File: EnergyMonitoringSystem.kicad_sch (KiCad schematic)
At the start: 0 parts

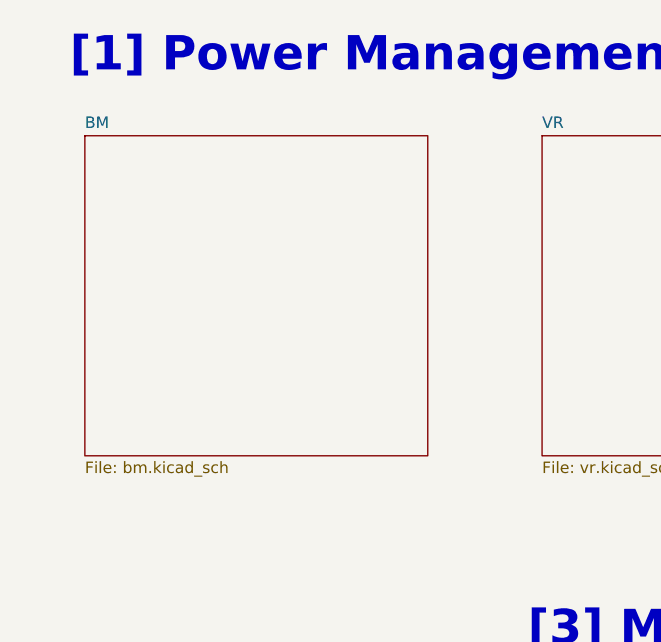
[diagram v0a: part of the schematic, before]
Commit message: only usb powered
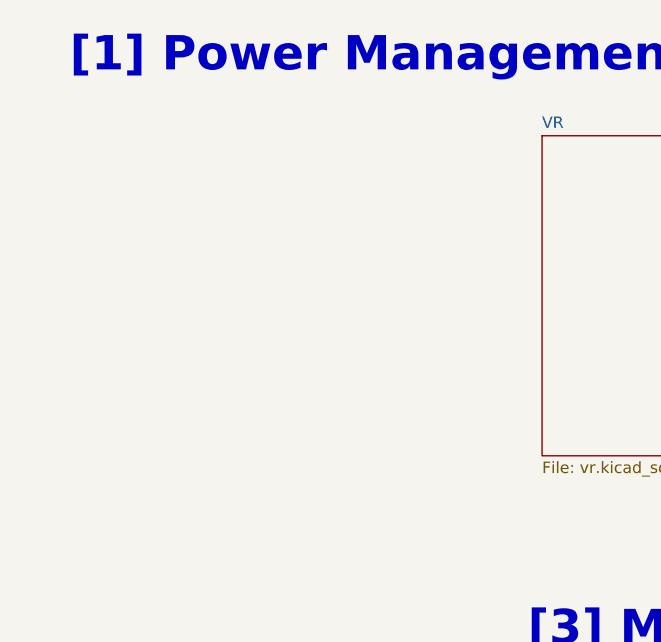
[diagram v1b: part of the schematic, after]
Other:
- removed sheet BM
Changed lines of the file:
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@@
 			(project "EnergyMonitoringSystem"
 				(path "/e660428c-c9b7-476c-8ac8-2d419f233469"
-					(page "7")
+					(page "6")
 				)
 			)
@@
 			(project "EnergyMonitoringSystem"
 				(path "/e660428c-c9b7-476c-8ac8-2d419f233469"
-					(page "4")
+					(page "2")
 				)
 			)
@@
 	)
 	(sheet
-		(at 25.4 36.83)
-		(size 38.1 35.56)
-		(fields_autoplaced yes)
-		(stroke
-			(width 0.1524)
-			(type solid)
-		)
-		(fill
-			(color 0 0 0 0.0000)
-		)
-		(property "Sheetname" "BM"
-			(at 25.4 36.1184 0)
-			(effects
-				(font
-					(size 1.27 1.27)
-				)
-				(justify left bottom)
-			)
-		)
-		(property "Sheetfile" "bm.kicad_sch"
-			(at 25.4 72.9746 0)
-			(effects
-				(font
-					(size 1.27 1.27)
-				)
-				(justify left top)
-			)
-		)
-		(instances
-			(project "EnergyMonitoringSystem"
-				(path "/e660428c-c9b7-476c-8ac8-2d419f233469"
-					(page "2")
-				)
-			)
-		)
-	)
-	(sheet
 		(at 76.2 99.06)
 		(size 39.37 36.83)
@@
 			(project "EnergyMonitoringSystem"
 				(path "/e660428c-c9b7-476c-8ac8-2d419f233469"
-					(page "6")
+					(page "4")
 				)
 			)

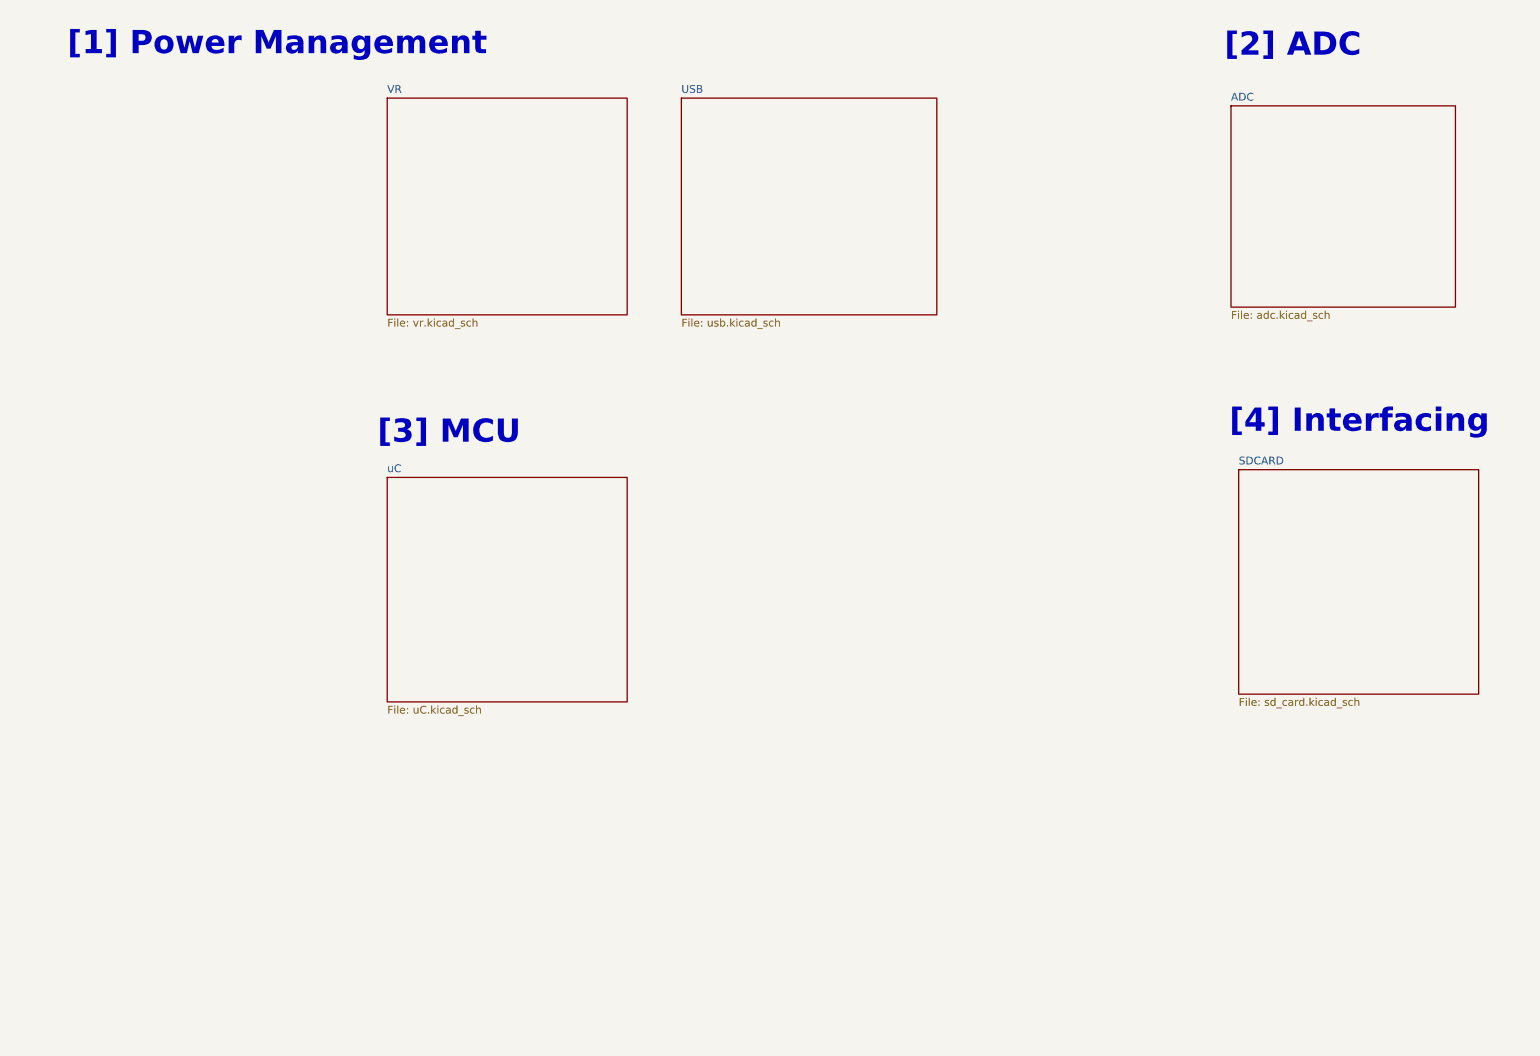
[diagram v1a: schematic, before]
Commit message: components with distributor links added
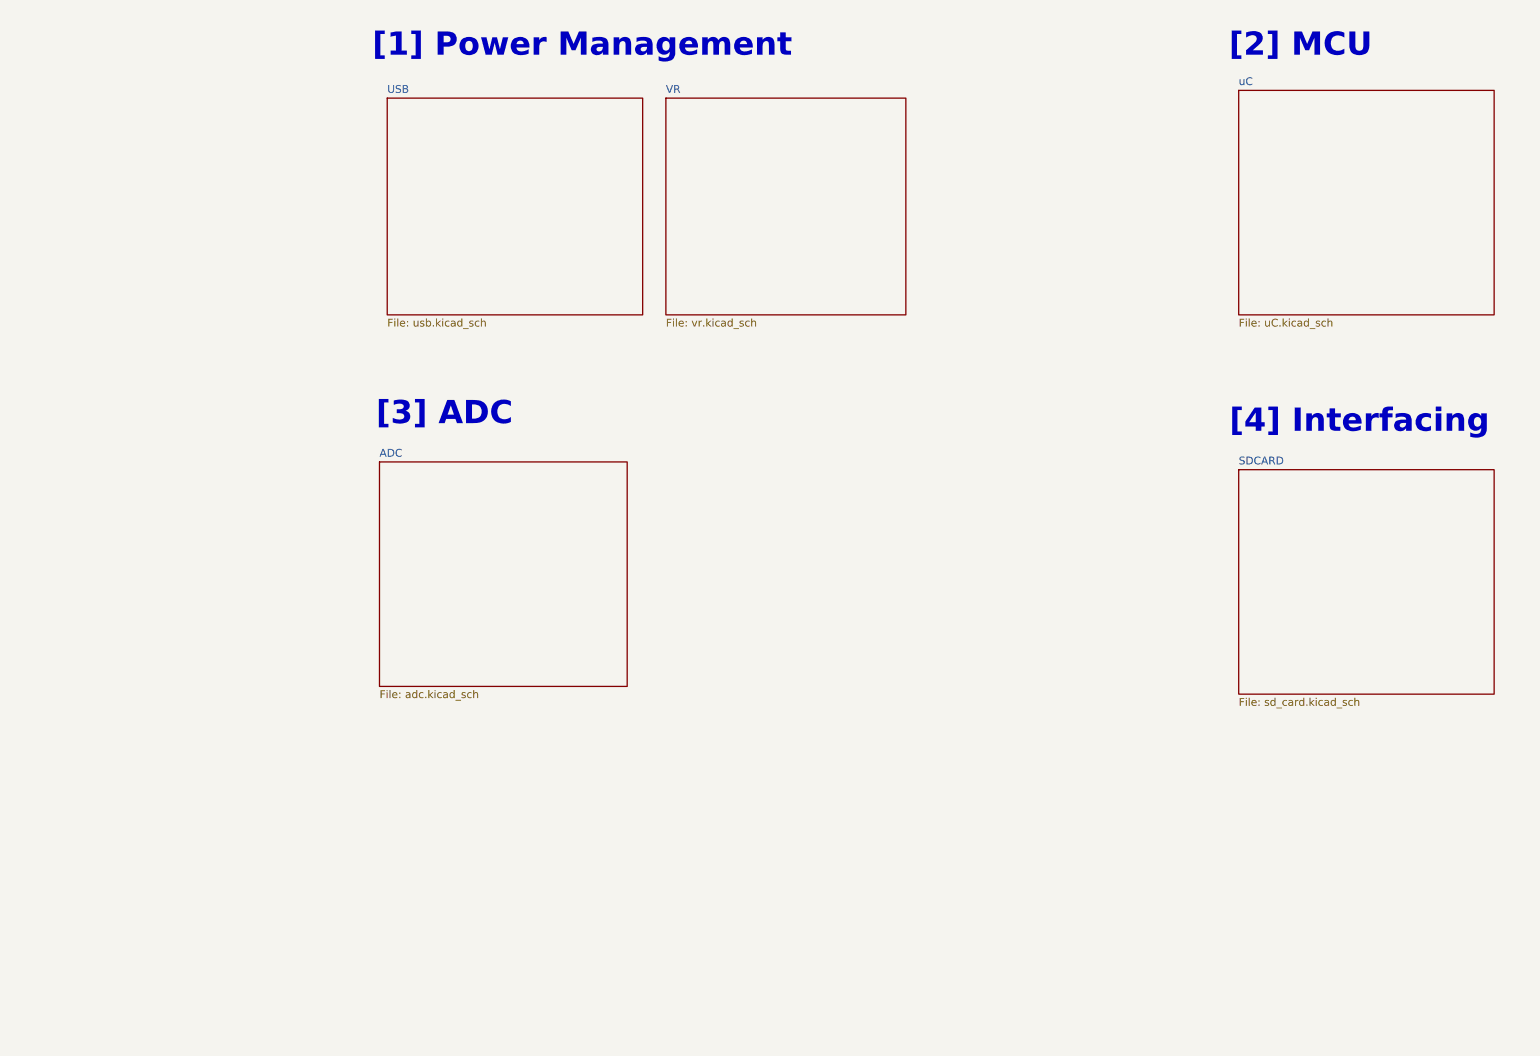
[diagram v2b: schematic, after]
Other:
- note added: "[2] MCU"
- note added: "[3] ADC"
- note removed: "[2] ADC"
- note removed: "[3] MCU"
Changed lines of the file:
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@@
 	(text "[1] Power Management\n"
 		(exclude_from_sim no)
-		(at 58.166 27.94 0)
-		(effects
-			(font
-				(size 3.81 3.81)
-				(thickness 1.016)
-				(bold yes)
-			)
-		)
-	)
-	(text "[2] ADC\n"
-		(exclude_from_sim no)
-		(at 224.79 28.194 0)
-		(effects
-			(font
-				(size 3.81 3.81)
-				(thickness 1.016)
-				(bold yes)
-			)
-		)
-	)
-	(text "[3] MCU\n"
-		(exclude_from_sim no)
-		(at 86.36 91.694 0)
+		(at 108.204 28.194 0)
+		(effects
+			(font
+				(size 3.81 3.81)
+				(thickness 1.016)
+				(bold yes)
+			)
+		)
+	)
+	(text "[3] ADC\n"
+		(exclude_from_sim no)
+		(at 85.598 88.646 0)
+		(effects
+			(font
+				(size 3.81 3.81)
+				(thickness 1.016)
+				(bold yes)
+			)
+		)
+	)
+	(text "[2] MCU\n"
+		(exclude_from_sim no)
+		(at 226.06 28.194 0)
 		(effects
 			(font
@@
 	(sheet
 		(at 215.9 97.79)
-		(size 39.37 36.83)
+		(size 41.91 36.83)
 		(fields_autoplaced yes)
 		(stroke
@@
 	)
 	(sheet
+		(at 121.92 36.83)
+		(size 39.37 35.56)
+		(fields_autoplaced yes)
+		(stroke
+			(width 0.1524)
+			(type solid)
+		)
+		(fill
+			(color 0 0 0 0.0000)
+		)
+		(property "Sheetname" "VR"
+			(at 121.92 36.1184 0)
+			(effects
+				(font
+					(size 1.27 1.27)
+				)
+				(justify left bottom)
+			)
+		)
+		(property "Sheetfile" "vr.kicad_sch"
+			(at 121.92 72.9746 0)
+			(effects
+				(font
+					(size 1.27 1.27)
+				)
+				(justify left top)
+			)
+		)
+		(instances
+			(project "EnergyMonitoringSystem"
+				(path "/e660428c-c9b7-476c-8ac8-2d419f233469"
+					(page "3")
+				)
+			)
+		)
+	)
+	(sheet
 		(at 76.2 36.83)
-		(size 39.37 35.56)
-		(fields_autoplaced yes)
-		(stroke
-			(width 0.1524)
-			(type solid)
-		)
-		(fill
-			(color 0 0 0 0.0000)
-		)
-		(property "Sheetname" "VR"
+		(size 41.91 35.56)
+		(fields_autoplaced yes)
+		(stroke
+			(width 0.1524)
+			(type solid)
+		)
+		(fill
+			(color 0 0 0 0.0000)
+		)
+		(property "Sheetname" "USB"
 			(at 76.2 36.1184 0)
 			(effects
@@
 			)
 		)
-		(property "Sheetfile" "vr.kicad_sch"
+		(property "Sheetfile" "usb.kicad_sch"
 			(at 76.2 72.9746 0)
 			(effects
@@
 			(project "EnergyMonitoringSystem"
 				(path "/e660428c-c9b7-476c-8ac8-2d419f233469"
-					(page "3")
-				)
-			)
-		)
-	)
-	(sheet
-		(at 124.46 36.83)
-		(size 41.91 35.56)
-		(fields_autoplaced yes)
-		(stroke
-			(width 0.1524)
-			(type solid)
-		)
-		(fill
-			(color 0 0 0 0.0000)
-		)
-		(property "Sheetname" "USB"
-			(at 124.46 36.1184 0)
-			(effects
-				(font
-					(size 1.27 1.27)
-				)
-				(justify left bottom)
-			)
-		)
-		(property "Sheetfile" "usb.kicad_sch"
-			(at 124.46 72.9746 0)
-			(effects
-				(font
-					(size 1.27 1.27)
-				)
-				(justify left top)
-			)
-		)
-		(instances
-			(project "EnergyMonitoringSystem"
-				(path "/e660428c-c9b7-476c-8ac8-2d419f233469"
 					(page "2")
 				)
@@
 	)
 	(sheet
-		(at 214.63 38.1)
-		(size 36.83 33.02)
+		(at 74.93 96.52)
+		(size 40.64 36.83)
 		(fields_autoplaced yes)
 		(stroke
@@
 		)
 		(property "Sheetname" "ADC"
-			(at 214.63 37.3884 0)
+			(at 74.93 95.8084 0)
 			(effects
 				(font
@@
 		)
 		(property "Sheetfile" "adc.kicad_sch"
-			(at 214.63 71.7046 0)
+			(at 74.93 133.9346 0)
 			(effects
 				(font
@@
 	)
 	(sheet
-		(at 76.2 99.06)
-		(size 39.37 36.83)
+		(at 215.9 35.56)
+		(size 41.91 36.83)
 		(fields_autoplaced yes)
 		(stroke
@@
 		)
 		(property "Sheetname" "uC"
-			(at 76.2 98.3484 0)
+			(at 215.9 34.8484 0)
 			(effects
 				(font
@@
 		)
 		(property "Sheetfile" "uC.kicad_sch"
-			(at 76.2 136.4746 0)
-			(effects
-				(font
+			(at 215.9 72.9746 0)
+			(effects
+				(font

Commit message: v2.0 started
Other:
- added sheet uCMain (uCMain.kicad_sch)
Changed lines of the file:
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@@
 			(project "EnergyMonitoringSystem"
 				(path "/e660428c-c9b7-476c-8ac8-2d419f233469"
-					(page "6")
+					(page "7")
 				)
 			)
@@
 			(effects
 				(font
+					(size 1.27 1.27)
+				)
+				(justify left top)
+			)
+		)
+		(instances
+			(project "EnergyMonitoringSystem"
+				(path "/e660428c-c9b7-476c-8ac8-2d419f233469"
+					(page "6")
+				)
+			)
+		)
+	)
+	(sheet
+		(at 127 96.52)
+		(size 38.1 36.83)
+		(fields_autoplaced yes)
+		(stroke
+			(width 0.1524)
+			(type solid)
+		)
+		(fill
+			(color 0 0 0 0.0000)
+		)
+		(property "Sheetname" "uCMain"
+			(at 127 95.8084 0)
+			(effects
+				(font
+					(size 1.27 1.27)
+				)
+				(justify left bottom)
+			)
+		)
+		(property "Sheetfile" "uCMain.kicad_sch"
+			(at 127 133.9346 0)
+			(effects
+				(font

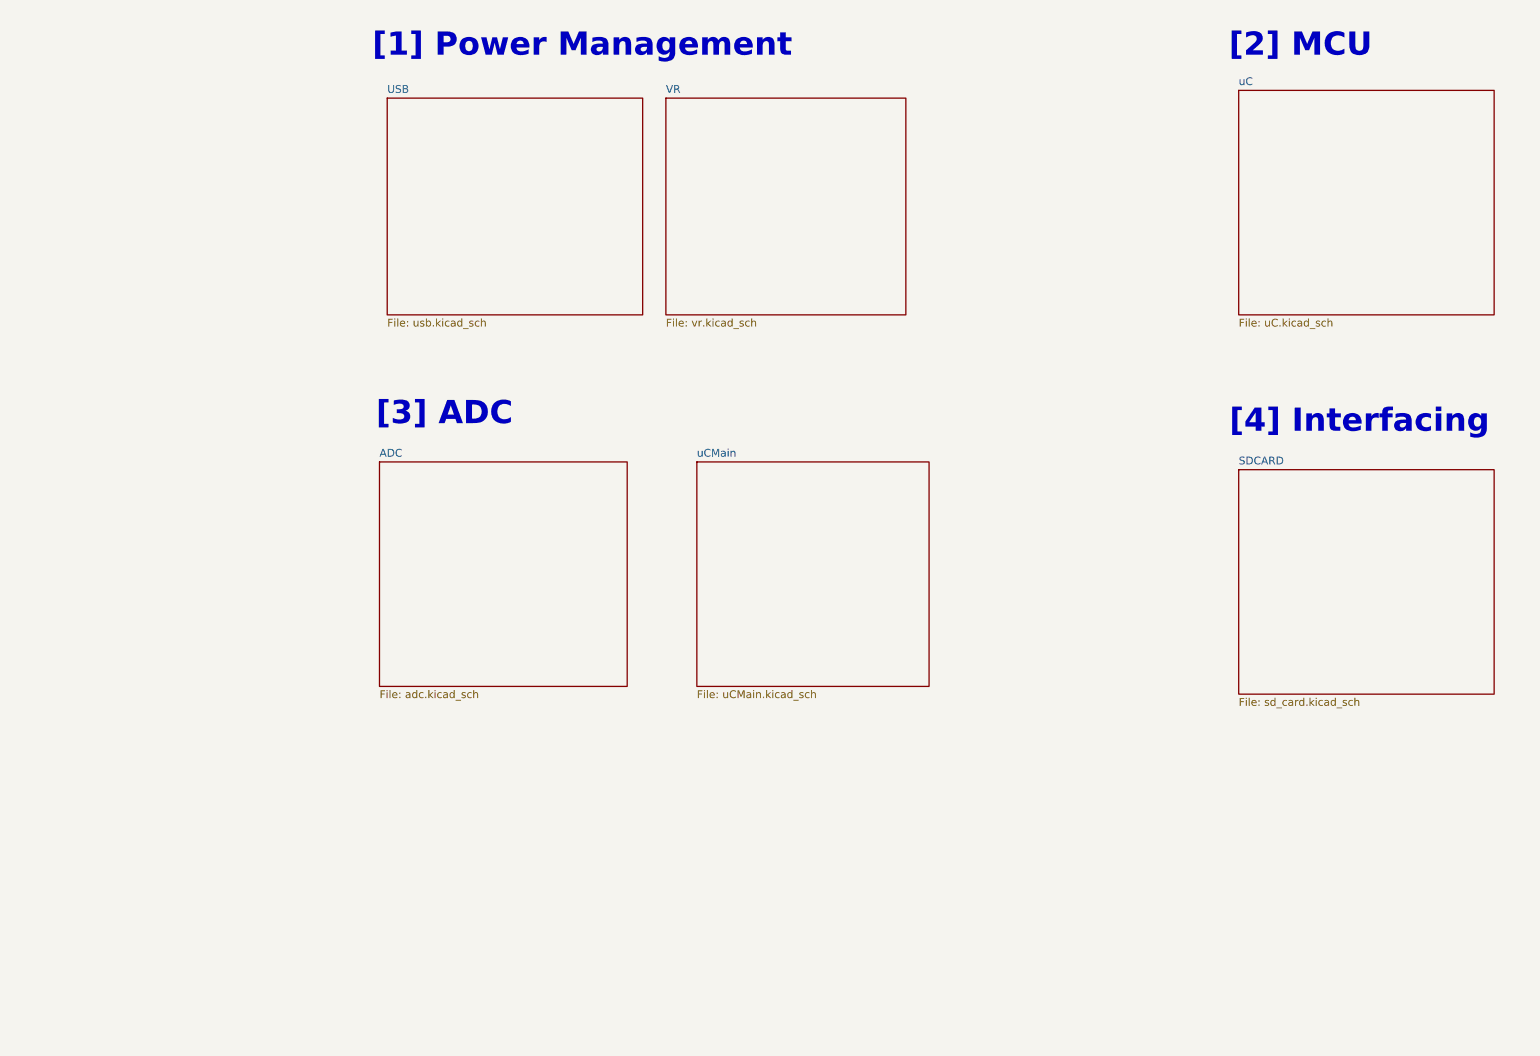
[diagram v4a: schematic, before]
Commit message: v2.0 schematics updated
1. Need to be tested for errors
2. PCB layout is not started yet
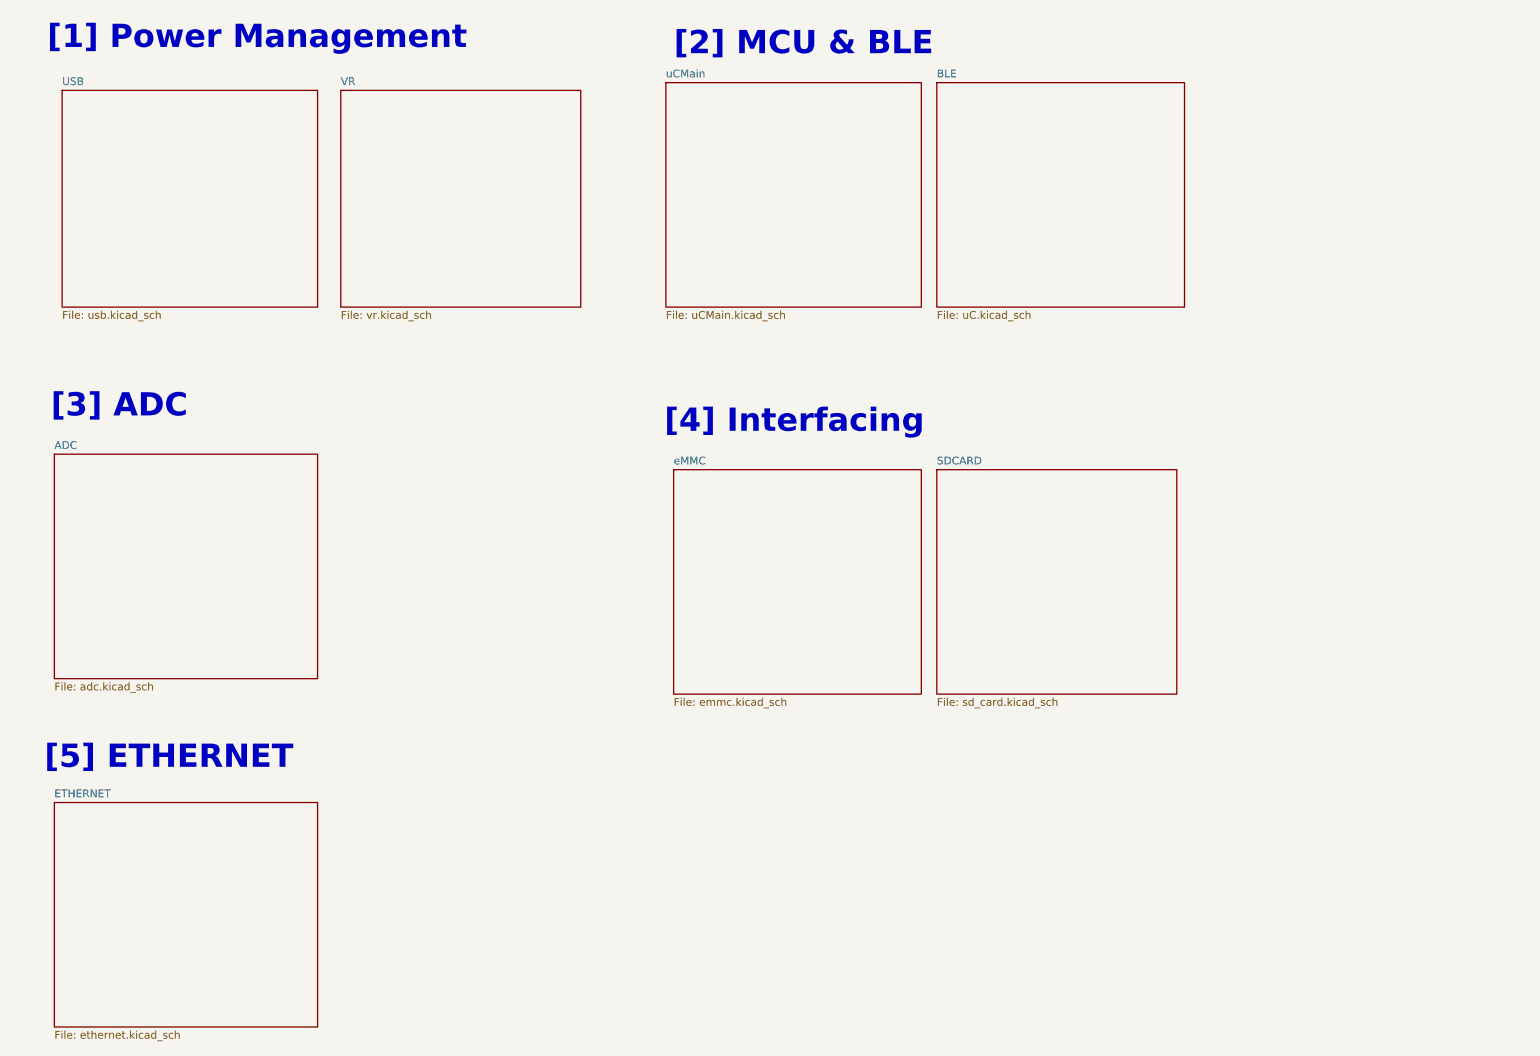
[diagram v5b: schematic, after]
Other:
- sheet uC renamed BLE
- added sheet ETHERNET (ethernet.kicad_sch)
- added sheet eMMC (emmc.kicad_sch)
- note added: "[2] MCU & BLE"
- note added: "[5] ETHERNET"
- note removed: "[2] MCU"
